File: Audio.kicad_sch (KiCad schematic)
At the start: 2 parts

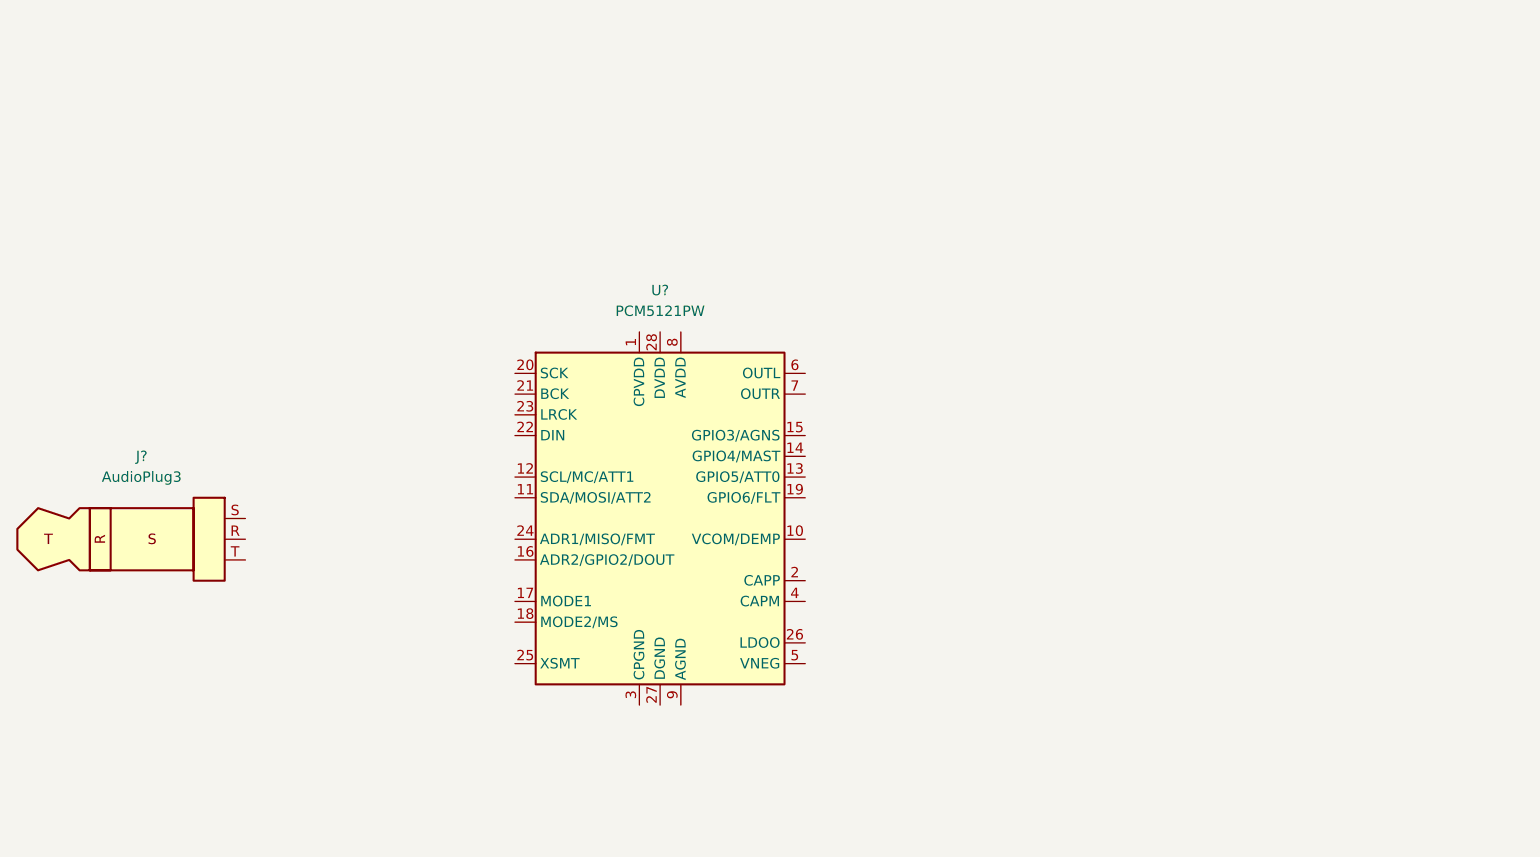
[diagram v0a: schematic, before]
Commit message: Wire up TI PCM5121 audio connect
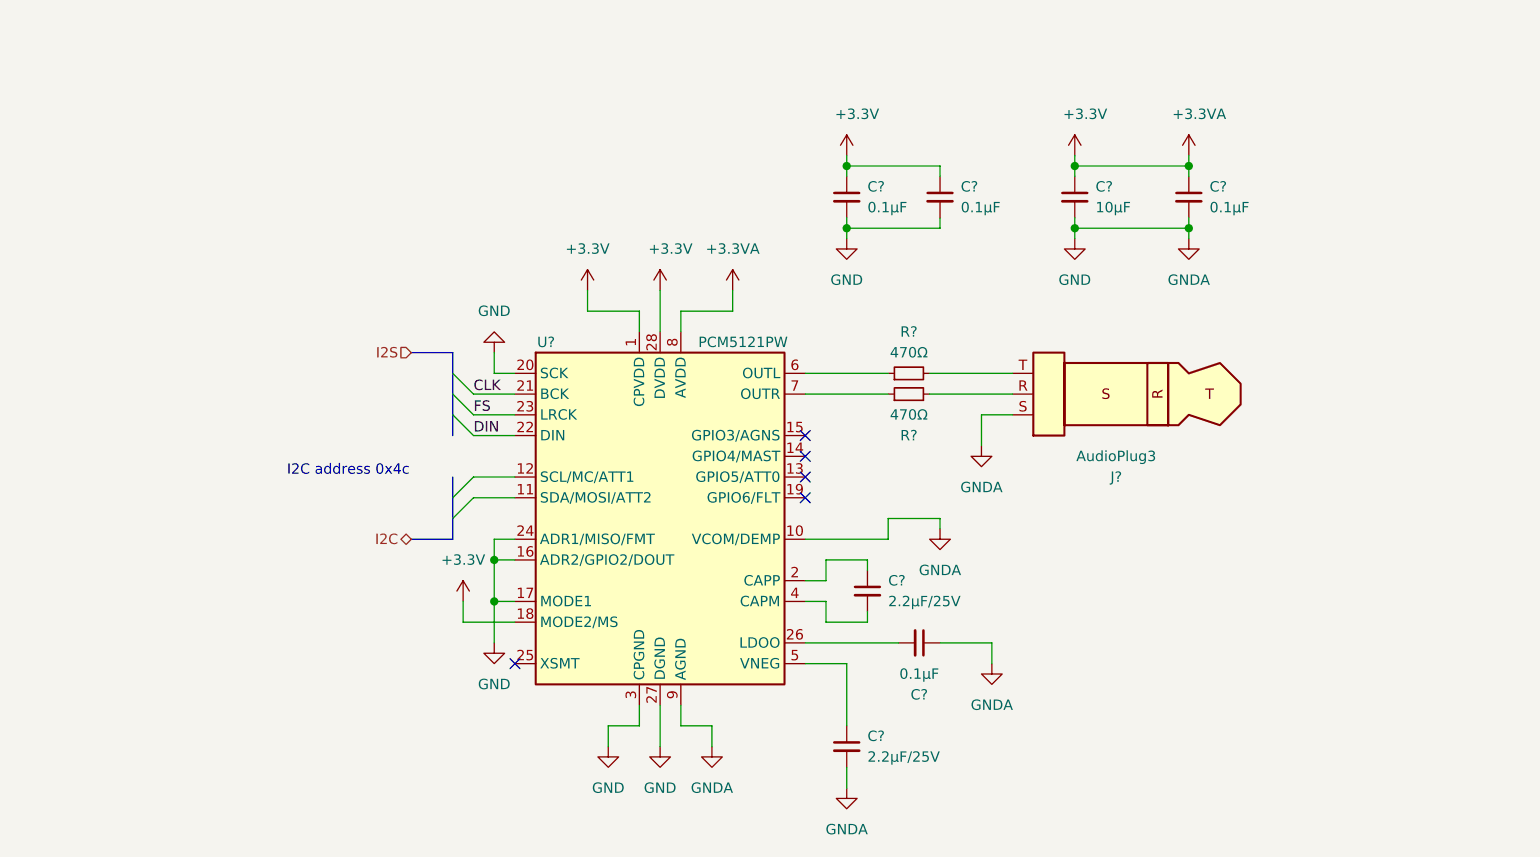
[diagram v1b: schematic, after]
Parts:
- added C? (x4): 0.1µF, symbol Device:C_Small
- added C?: 10µF, symbol Device:C_Small
- added C? (x2): 2.2µF/25V, symbol Device:C_Small
- added R? (x2): 470Ω, symbol Device:R_Small
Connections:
- net +3.3VA: now reaches U?.1 (CPVDD)
- net +3.3VA: now also U?.18 (MODE2/MS), U?.28 (DVDD), U?.8 (AVDD), C?.1, C?.1, C?.1, C?.1
- net GND: now reaches U?.10 (VCOM/DEMP)
- net GND: now also J?.S, U?.16 (ADR2/GPIO2/DOUT), U?.17 (MODE1), U?.20 (SCK), U?.24 (ADR1/MISO/FMT), U?.27 (DGND), U?.3 (CPGND), U?.9 (AGND), C?.1, C?.2, C?.2, C?.2, C?.2, C?.2
- net at U?.2 (CAPP): now also C?.1
- net CLK: now reaches U?.21 (BCK)
- net DIN: now reaches U?.22 (DIN)
- net FS: now reaches U?.23 (LRCK)
- net at U?.26 (LDOO): now also C?.2
- net at U?.4 (CAPM): now also C?.2
- net at U?.5 (VNEG): now also C?.1
- net at U?.6 (OUTL): now also R?.1
- net at U?.7 (OUTR): now also R?.1
- net at J?.R: now also R?.2
- net at J?.T: now also R?.2
- no-connect marks 0 -> 5
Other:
- note added: "I2C address 0x4c"
- moved on the sheet: J?

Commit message: Multiple changes in schematic & projects:
    -Added net classes for controlled impedance traces
    -Added power hierarchical sheet
    -Initial USB subsystem schematic
    -Added multiple bus definitions (usb, pcie, i2c etc.)
    -Fixed busses use
    -Added LDO for audio analog rails

Signed-off-by: Dominik Sliwa <dominik@sliwa.io>
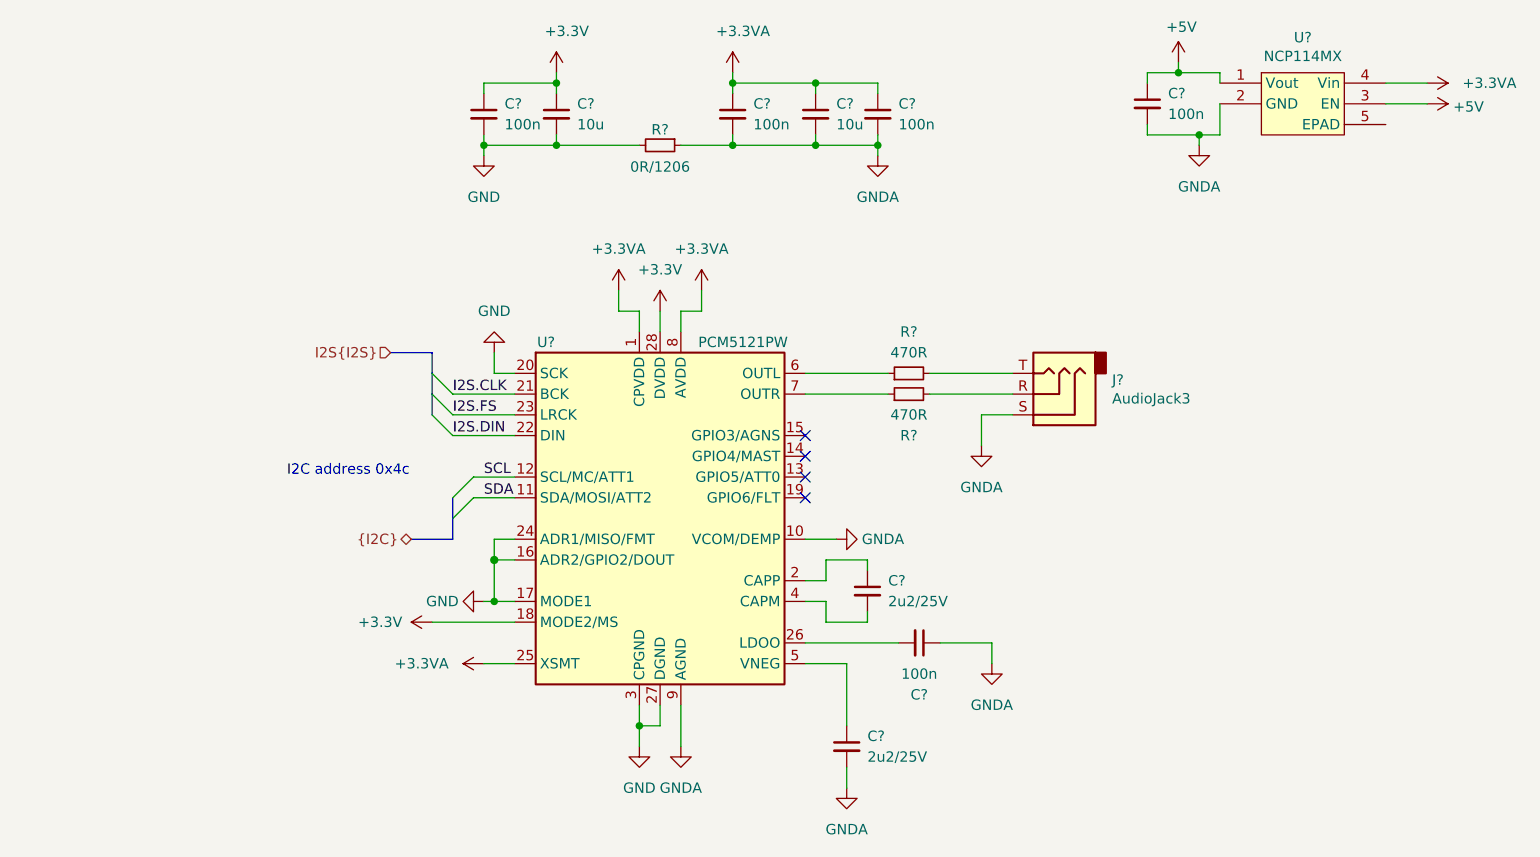
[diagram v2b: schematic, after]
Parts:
- removed C?: 0.1µF, symbol Device:C_Small
- removed J?: AudioPlug3, symbol Connector:AudioPlug3
- added C? (x2): 100n, symbol Device:C_Small
- added C?: 10u, symbol Device:C_Small
- added J?: AudioJack3, symbol Connector:AudioJack3
- added R?: 0R/1206, symbol Device:R_Small
- added U?: NCP114MX, symbol custom:NCP114MX
- C? (x3): value 0.1µF -> 100n
- C?: value 10µF -> 10u
- C? (x2): value 2.2µF/25V -> 2u2/25V
- R? (x2): value 470Ω -> 470R
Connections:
- net +3.3VA: now also U?.25 (XSMT), C?.1, C?.1, U?.4 (Vin); no longer C?.1, C?.1, U?.18 (MODE2/MS), U?.28 (DVDD)
- net GND: now also R?.2; no longer C?.1, C?.2, C?.2, U?.10 (VCOM/DEMP), U?.9 (AGND)
- net SDA: now reaches U?.11 (SDA/MOSI/ATT2)
- net SCL: now reaches U?.12 (SCL/MC/ATT1)
- net at R?.2: now also J?.R
- net at R?.2: now also J?.T
- net CLK renamed I2S.CLK
- net DIN renamed I2S.DIN
- net FS renamed I2S.FS
- new net +3V3: C?.1, C?.1, U?.18 (MODE2/MS), U?.28 (DVDD)
- new net +5V: C?.1, U?.1 (Vout), U?.3 (EN)
- new net GNDA: C?.1, C?.2, C?.2, C?.2, C?.2, C?.2, J?.S, R?.1, U?.10 (VCOM/DEMP), U?.2 (GND), U?.9 (AGND)
- no-connect marks 5 -> 4
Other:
- moved on the sheet: C?

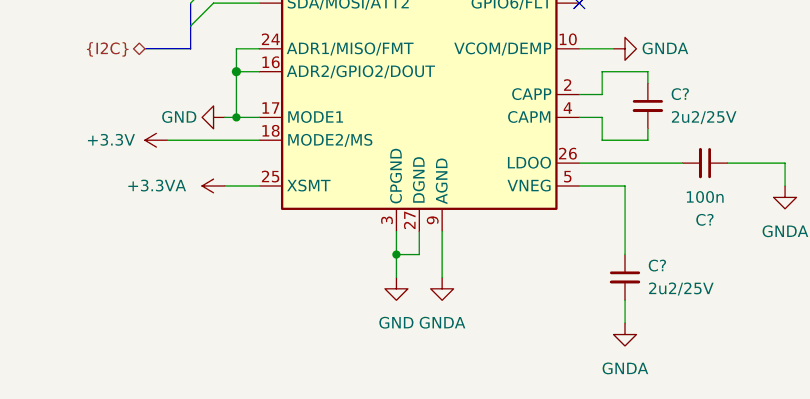
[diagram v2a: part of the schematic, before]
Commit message: Changes:     -Added AP64501SP-13 library symbol     -Initial power supplies schematics     -Increased capacitance for PCIe socket     -Connections between sheets
Signed-off-by: Dominik Sliwa <dominik@sliwa.io>
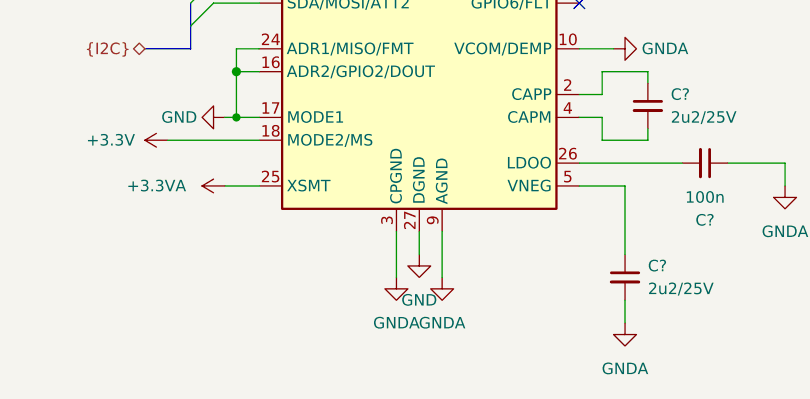
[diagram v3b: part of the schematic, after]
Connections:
- net GND: no longer U?.3 (CPGND)
- net GNDA: now also U?.3 (CPGND)
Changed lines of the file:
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@@
   (junction (at 132.08 40.64) (diameter 0.9144) (color 0 0 0 0))
   (junction (at 132.08 48.26) (diameter 0.9144) (color 0 0 0 0))
-  (junction (at 142.24 119.38) (diameter 0.9144) (color 0 0 0 0))
   (junction (at 153.67 40.64) (diameter 0.9144) (color 0 0 0 0))
   (junction (at 153.67 48.26) (diameter 0.9144) (color 0 0 0 0))
@@
   (junction (at 208.28 39.37) (diameter 0.9144) (color 0 0 0 0))
   (junction (at 210.82 46.99) (diameter 0.9144) (color 0 0 0 0))
+  (no_connect (at 162.56 91.44))
+  (no_connect (at 162.56 83.82))
   (no_connect (at 162.56 88.9))
-  (no_connect (at 162.56 83.82))
   (no_connect (at 162.56 86.36))
-  (no_connect (at 162.56 91.44))
   (bus_entry (at 116.84 76.2) (size 2.54 2.54)
     (stroke (width 0.1524) (type solid) (color 0 0 0 0))
@@
     (stroke (width 0) (type solid) (color 0 0 0 0))
   )
-  (wire (pts (xy 142.24 116.84) (xy 142.24 119.38))
-    (stroke (width 0) (type solid) (color 0 0 0 0))
-  )
-  (wire (pts (xy 142.24 119.38) (xy 142.24 121.92))
-    (stroke (width 0) (type solid) (color 0 0 0 0))
-  )
-  (wire (pts (xy 142.24 119.38) (xy 144.78 119.38))
+  (wire (pts (xy 142.24 116.84) (xy 142.24 121.92))
     (stroke (width 0) (type solid) (color 0 0 0 0))
   )
@@
     )
   )
-  (symbol (lib_id "power:GND") (at 142.24 121.92 0) (unit 1)
+  (symbol (lib_id "power:GNDA") (at 142.24 121.92 0) (unit 1)
     (in_bom yes) (on_board yes)
     (property "Reference" "#PWR?" (id 0) (at 142.24 128.27 0)
       (effects (font (size 1.27 1.27)) hide)
     )
-    (property "Value" "GND" (id 1) (at 142.24 127 0))
+    (property "Value" "GNDA" (id 1) (at 142.24 127 0))
     (property "Footprint" "" (id 2) (at 142.24 121.92 0)
       (effects (font (size 1.27 1.27)) hide)
@@
       (effects (font (size 1.27 1.27)) hide)
     )
+  )
+  (symbol (lib_id "power:GND") (at 144.78 119.38 0) (unit 1)
+    (in_bom yes) (on_board yes)
+    (property "Reference" "#PWR?" (id 0) (at 144.78 125.73 0)
+      (effects (font (size 1.27 1.27)) hide)
+    )
+    (property "Value" "GND" (id 1) (at 144.78 124.46 0))
+    (property "Footprint" "" (id 2) (at 144.78 119.38 0)
+      (effects (font (size 1.27 1.27)) hide)
+    )
+    (property "Datasheet" "" (id 3) (at 144.78 119.38 0)
+      (effects (font (size 1.27 1.27)) hide)
+    )

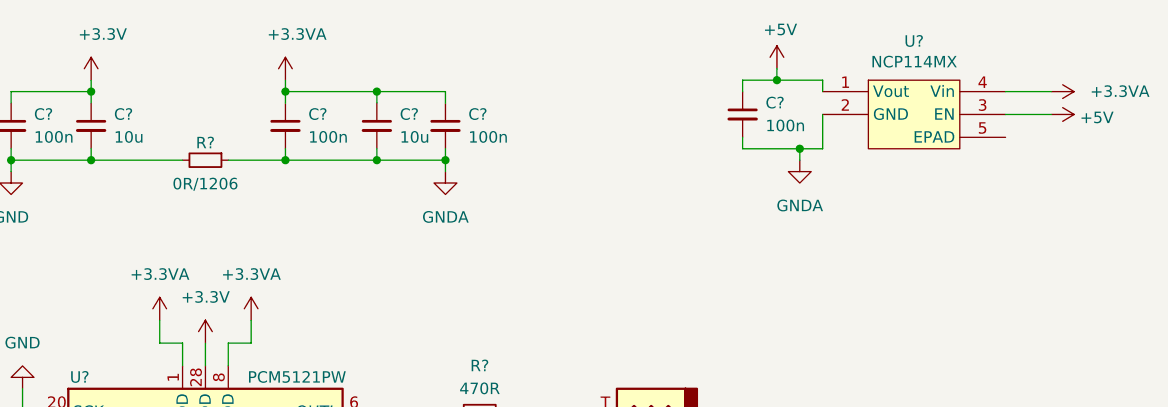
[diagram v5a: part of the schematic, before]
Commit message: PoE and clean-up
- Moved PoE to a seperate sheet and finished design
- Started using Config field for Variants and DNP flag
- Fix-ups
- Added Wurth 749119550 and TI TPS23734 to the symbol library
- Changed RTC from PCF8563 to PCF85063

Signed-off-by: Dominik Sliwa <dominik@sliwa.io>
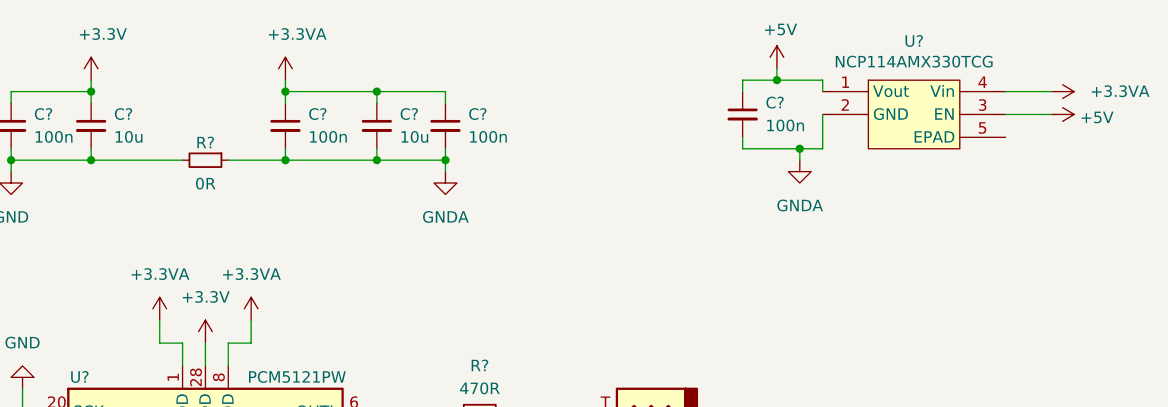
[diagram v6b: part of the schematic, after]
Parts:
- R?: value 0R/1206 -> 0R
- U?: value NCP114MX -> NCP114AMX330TCG
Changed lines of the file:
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@@
   (junction (at 208.28 39.37) (diameter 0.9144) (color 0 0 0 0))
   (junction (at 210.82 46.99) (diameter 0.9144) (color 0 0 0 0))
+  (no_connect (at 162.56 91.44))
   (no_connect (at 162.56 88.9))
   (no_connect (at 162.56 86.36))
-  (no_connect (at 162.56 91.44))
   (no_connect (at 162.56 83.82))
   (bus_entry (at 116.84 76.2) (size 2.54 2.54)
@@
     (in_bom yes) (on_board yes)
     (property "Reference" "R?" (id 0) (at 144.78 46.3488 90))
-    (property "Value" "0R/1206" (id 1) (at 144.78 50.908 90))
+    (property "Value" "0R" (id 1) (at 144.78 50.908 90))
     (property "Footprint" "" (id 2) (at 144.78 48.26 0)
       (effects (font (size 1.27 1.27)) hide)
@@
     (in_bom yes) (on_board yes)
     (property "Reference" "U?" (id 0) (at 223.52 35.0582 0))
-    (property "Value" "NCP114MX" (id 1) (at 223.52 37.3569 0))
+    (property "Value" "NCP114AMX330TCG" (id 1) (at 223.52 37.3569 0))
     (property "Footprint" "" (id 2) (at 223.52 41.91 0)
       (effects (font (size 1.27 1.27)) hide)
     )
-    (property "Datasheet" "" (id 3) (at 223.52 41.91 0)
-      (effects (font (size 1.27 1.27)) hide)
-    )
+    (property "Datasheet" "https://www.onsemi.com/pub/Collateral/NCP114-D.PDF" (id 3) (at 223.52 41.91 0)
+      (effects (font (size 1.27 1.27)) hide)
+    )
